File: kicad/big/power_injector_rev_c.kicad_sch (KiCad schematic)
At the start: 27 parts, among them J2 A00-108-220-450, J3 A00-108-220-450, J4 JACK-PLUG0, X1 22-23-2041, X10 22-23-2041, X11 22-23-2041, X12 22-23-2041, X13 22-23-2041, X14 22-23-2041, X15 22-23-2041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

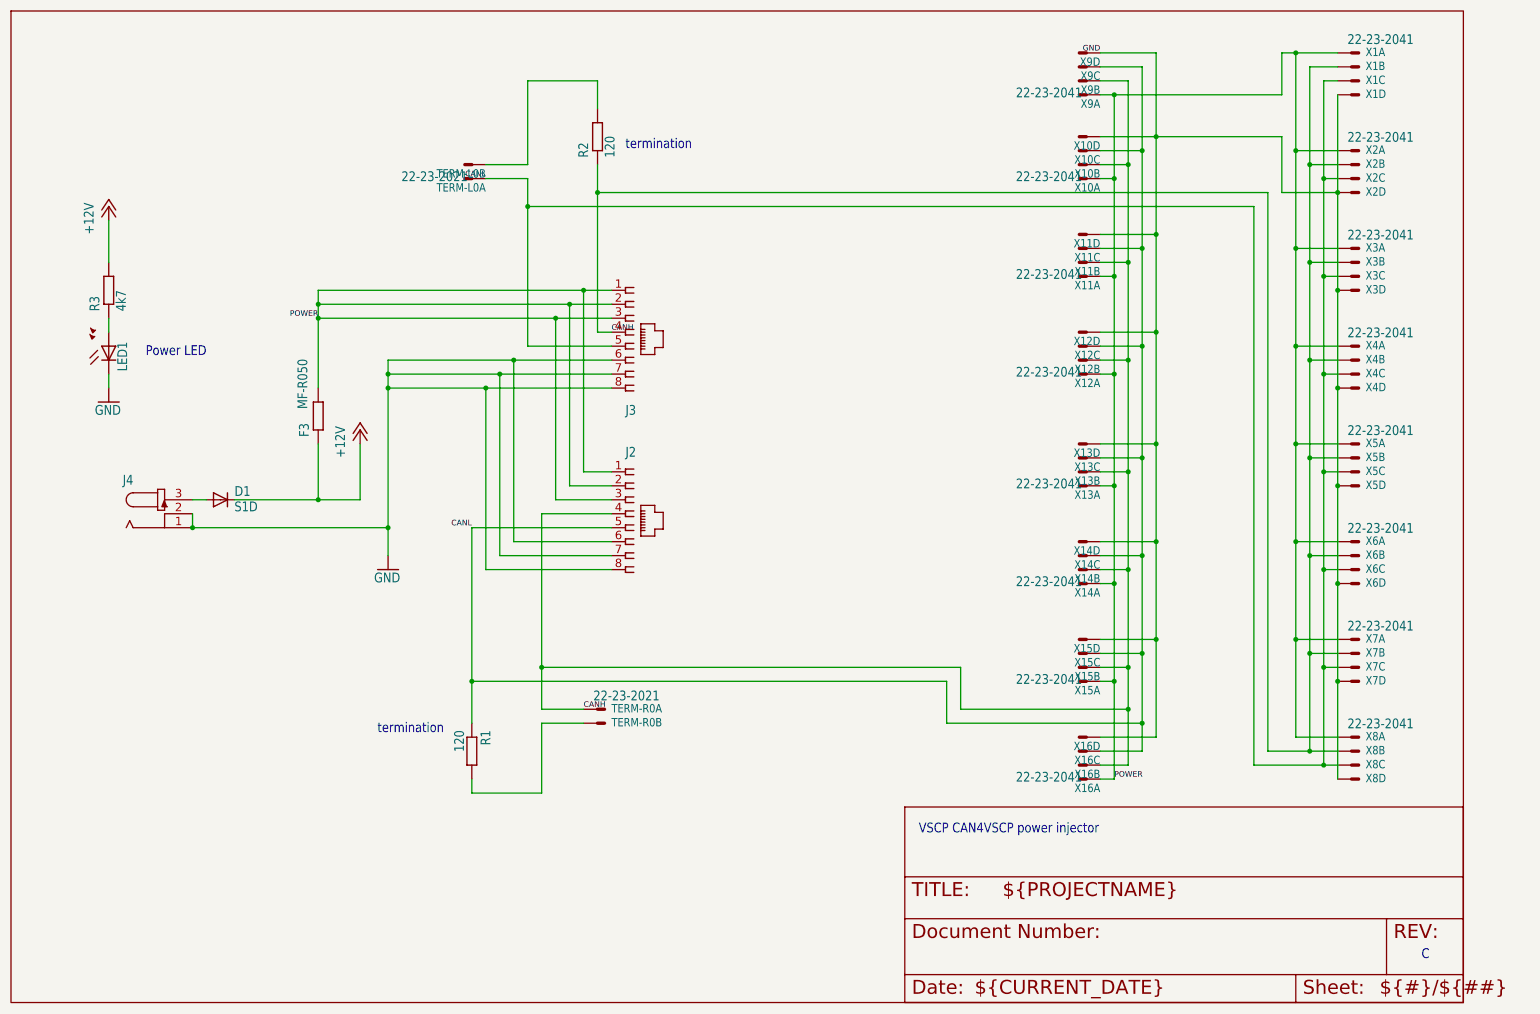
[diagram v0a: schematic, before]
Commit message: Rearranged files (in a more logical way)
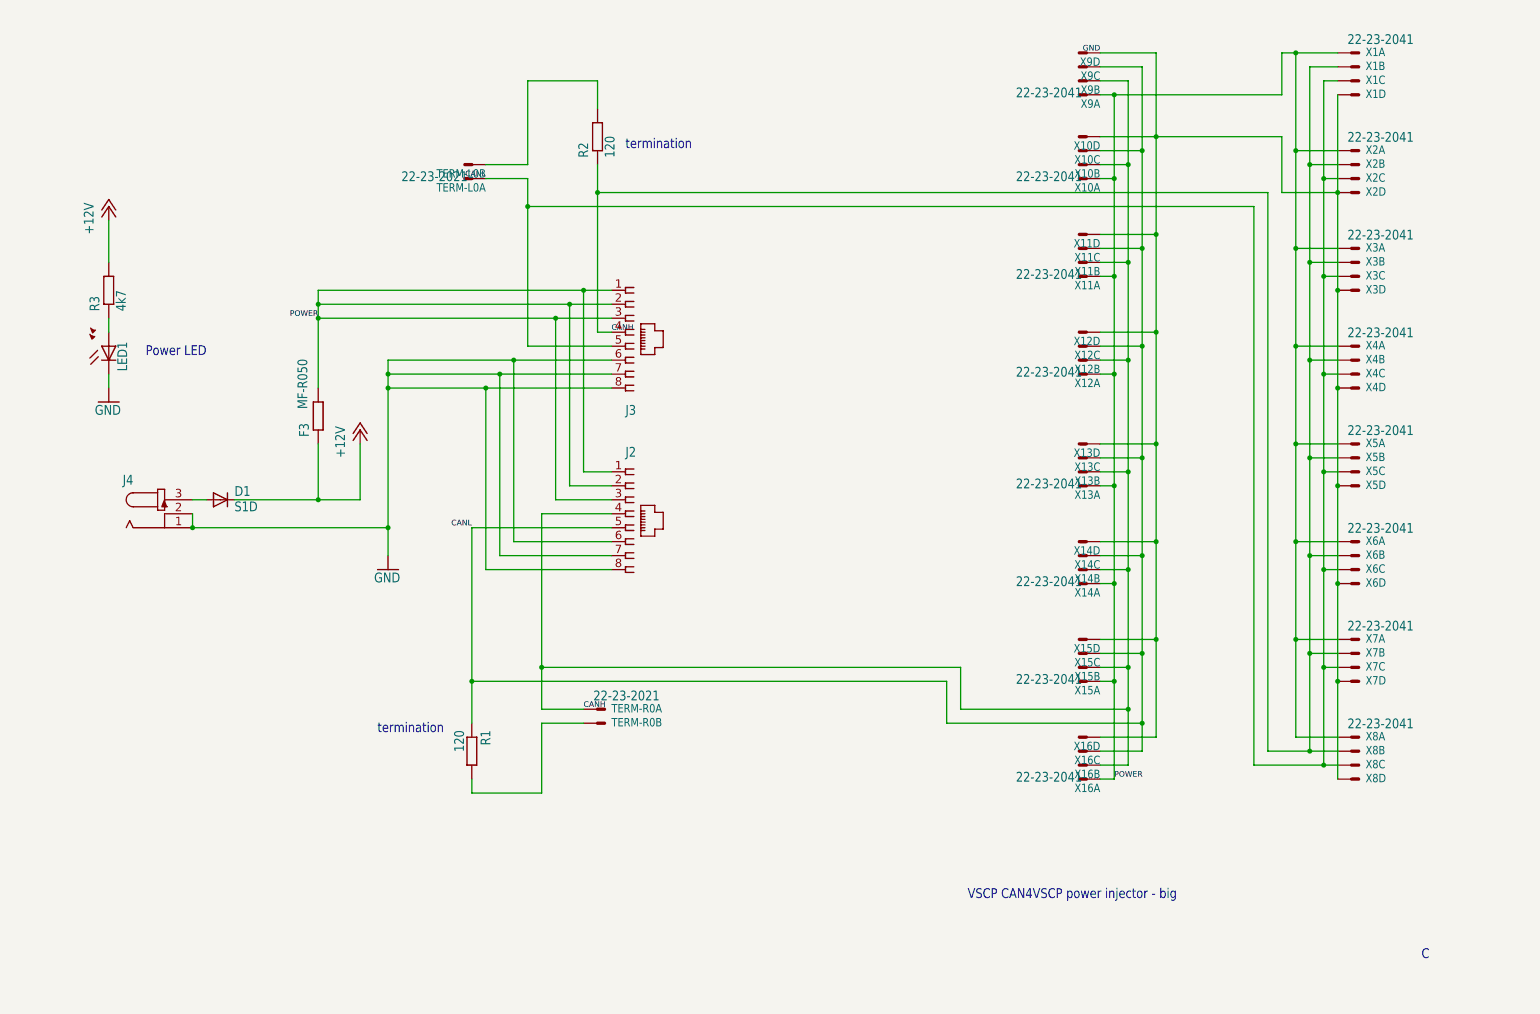
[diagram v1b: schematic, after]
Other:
- note added: "VSCP CAN4VSCP power injector - big"
- note removed: "VSCP CAN4VSCP power injector"
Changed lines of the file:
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@@
 		)
 	)
-	(text "VSCP CAN4VSCP power injector"
+	(text "VSCP CAN4VSCP power injector - big"
 		(exclude_from_sim no)
-		(at 182.88 167.64 0)
+		(at 191.77 179.578 0)
 		(effects
 			(font
@@
 	)
 	(symbol
-		(lib_id "power_injector_rev_c-eagle-import:DINA4_L")
-		(at 17.78 198.12 0)
-		(unit 1)
-		(exclude_from_sim no)
-		(in_bom yes)
-		(on_board yes)
-		(dnp no)
-		(property "Reference" "#FRAME1"
-			(at 17.78 198.12 0)
-			(effects
-				(font
-					(size 1.27 1.27)
-				)
-				(hide yes)
-			)
-		)
-		(property "Value" "DINA4_L"
-			(at 17.78 198.12 0)
-			(effects
-				(font
-					(size 1.27 1.27)
-				)
-				(hide yes)
-			)
-		)
-		(property "Footprint" ""
-			(at 17.78 198.12 0)
-			(effects
-				(font
-					(size 1.27 1.27)
-				)
-				(hide yes)
-			)
-		)
-		(property "Datasheet" ""
-			(at 17.78 198.12 0)
-			(effects
-				(font
-					(size 1.27 1.27)
-				)
-				(hide yes)
-			)
-		)
-		(property "Description" ""
-			(at 17.78 198.12 0)
-			(effects
-				(font
-					(size 1.27 1.27)
-				)
-				(hide yes)
-			)
-		)
-		(instances
-			(project ""
-				(path "/9869746d-4b47-4a0d-aa5e-3b217217de94"
-					(reference "#FRAME1")
-					(unit 1)
-				)
-			)
-		)
-	)
-	(symbol
 		(lib_id "power_injector_rev_c-eagle-import:22-23-2041")
 		(at 213.36 78.74 180)
@@
 				)
 			)
-		)
-	)
-	(symbol
-		(lib_id "power_injector_rev_c-eagle-import:DINA4_L")
-		(at 180.34 198.12 0)
-		(unit 2)
-		(exclude_from_sim no)
-		(in_bom yes)
-		(on_board yes)
-		(dnp no)
-		(property "Reference" "#FRAME1"
-			(at 180.34 198.12 0)
-			(effects
-				(font
-					(size 1.27 1.27)
-				)
-				(hide yes)
-			)
-		)
-		(property "Value" "DINA4_L"
-			(at 180.34 198.12 0)
-			(effects
-				(font
-					(size 1.27 1.27)
-				)
-				(hide yes)
-			)
-		)
-		(property "Footprint" ""
-			(at 180.34 198.12 0)
-			(effects
-				(font
-					(size 1.27 1.27)
-				)
-				(hide yes)
-			)
-		)
-		(property "Datasheet" ""
-			(at 180.34 198.12 0)
-			(effects
-				(font
-					(size 1.27 1.27)
-				)
-				(hide yes)
-			)
-		)
-		(property "Description" ""
-			(at 180.34 198.12 0)
-			(effects
-				(font
-					(size 1.27 1.27)
-				)
-				(hide yes)
-			)
-		)
-		(instances
-			(project ""
-				(path "/9869746d-4b47-4a0d-aa5e-3b217217de94"
-					(reference "#FRAME1")
-					(unit 2)
-				)
-			)
